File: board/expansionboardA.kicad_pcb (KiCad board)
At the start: 2 copper layers, 131 x 83.8 mm, 83 parts, among them J1 USB_C_Receptacle, J2 USB_A_Stacked, J3 HDMI_A, J4 USB_C_Receptacle, SW1 ESPPROG, U1 MAX3420EECJ, U2 GPIO_U2, U3 SII164CTG64, U4 GPIO_U4, U5 ESP32-C6-WROOM-1-N8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

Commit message: Updated board with 2 more pins between ESP32 and FPGA
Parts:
- SW1: moved to B.Cu
- moved REF** 18.4 mm to (65.0, 100.2)
- moved SW1 3.72 mm to (75.2, 118.8)
- moved REF** 3.04 mm to (35.8, 119.8)
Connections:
- U2 pad 25: unconnected-(U2-Pin_25-Pad25) -> IO11
- U2 pad 26: unconnected-(U2-Pin_26-Pad26) -> IO10
- U5 pad 11: unconnected-(U5-IO10-Pad11) -> IO10
- U5 pad 12: unconnected-(U5-IO11-Pad12) -> IO11
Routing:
- net IO11: track 0.00 -> 13.3 mm
- net IO10: track 0.00 -> 11.5 mm
- net REG3V3: track 340.7 -> 342.1 mm
- net Net-(U5-IO9): track 43.5 -> 42.4 mm, vias 1 -> 2
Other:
- board text added: "ESP32 DOWNLOAD"
- board text added: "K13"
- board text added: "K14"
- board text removed: "ESP32 DOWNLOAD MODE"

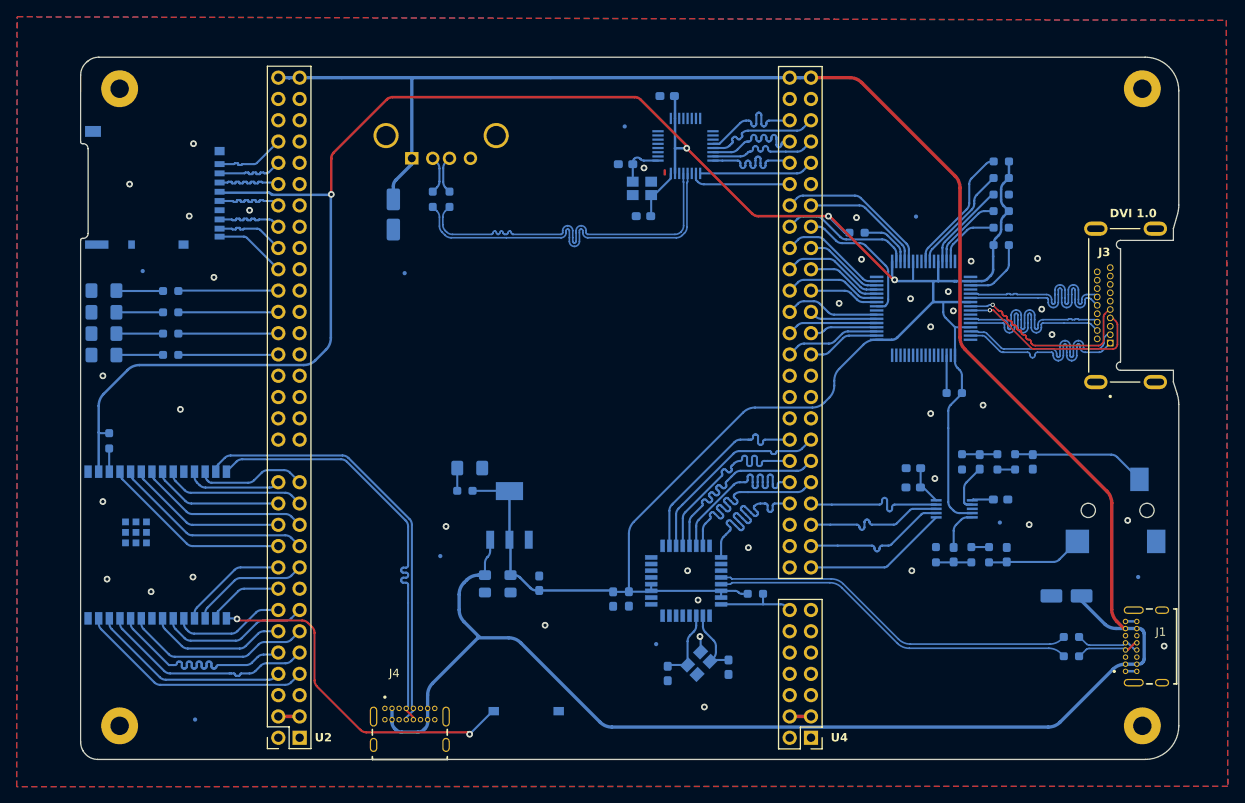
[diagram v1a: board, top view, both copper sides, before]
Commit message: Updated gateware, ROM version, and board schematic to remove MAX3420 support
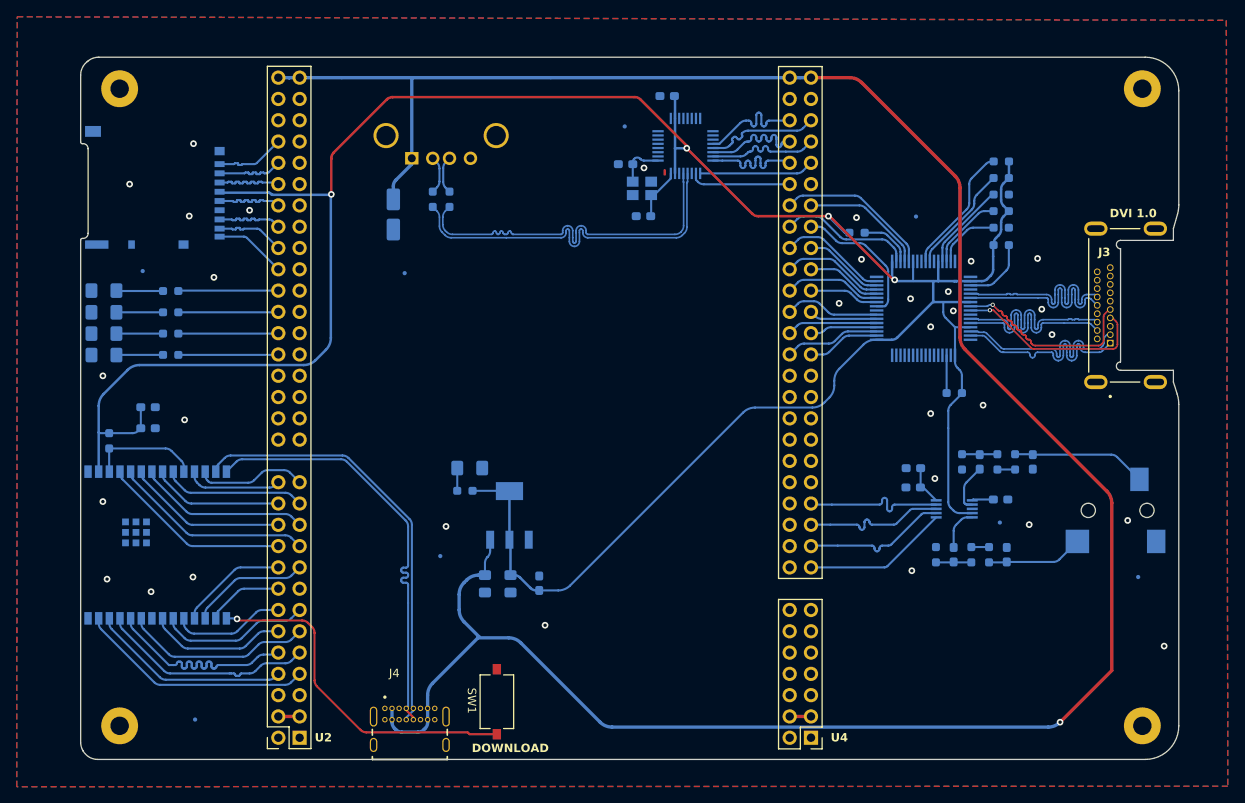
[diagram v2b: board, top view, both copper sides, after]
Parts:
- removed C3, C4: 18pf, Capacitor_SMD:C_0603_1608Metric_Pad1.08x0.95mm_HandSolder
- removed C5: 4.7uf, Capacitor_SMD:CP_Elec_4x5.4
- removed J1: USB_C_Receptacle, USB4085-GF-A_REVA4:GCT_USB4085-GF-A_REVA4
- removed R10, R9: 33Ohm, Resistor_SMD:R_0603_1608Metric_Pad0.98x0.95mm_HandSolder
- removed R2: 10KOhm, Resistor_SMD:R_0603_1608Metric_Pad0.98x0.95mm_HandSolder
- removed the REF** at (90.8, 110.8)
- removed U1: MAX3420EECJ, MAX3420EECJ:QFP80P900X900X160-32N
- removed Y1: 403C35D12M00000, 403C35D12M00000:XTAL_403C35D12M00000
- SW1: moved to F.Cu
- moved C2 60.9 mm to (30.1, 85.0), turned to 180 degrees
- moved C1 60.0 mm to (30.1, 82.5), turned to 180 degrees
- moved SW1 3.68 mm to (71.8, 117.6), turned to -90 degrees
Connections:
- U4 pad 24: INT -> unconnected-(U4-Pin_24-Pad24)
- U4 pad 25: USBGPX -> unconnected-(U4-Pin_25-Pad25)
- U4 pad 26: USBMOSI -> unconnected-(U4-Pin_26-Pad26)
- U4 pad 27: USBMISO -> unconnected-(U4-Pin_27-Pad27)
- U4 pad 28: USBSS -> unconnected-(U4-Pin_28-Pad28)
- U4 pad 29: USBSCLK -> unconnected-(U4-Pin_29-Pad29)
- U4 pad 30: USBRES -> unconnected-(U4-Pin_30-Pad30)
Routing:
- net USBD_P: track 44.3 -> 0.00 mm
- net USBD_N: track 44.2 -> 0.00 mm
- net USBSCLK: track 24.0 -> 0.00 mm
- net USBRES: track 24.0 -> 0.00 mm
- net USBGPX: track 23.9 -> 0.00 mm
- net USBMISO: track 23.9 -> 0.00 mm
- net USBMOSI: track 23.9 -> 0.00 mm
- net USBSS: track 23.9 -> 0.00 mm
- net INT: track 23.8 -> 0.00 mm
- net REG3V3: track 342.1 -> 328.0 mm
- net 5V: track 296.9 -> 284.4 mm, vias 0 -> 1
- net Net-(U5-EN): track 2.78 -> 13.3 mm
- net GPI: track 9.66 -> 0.00 mm
- net Net-(U1-XI): track 8.77 -> 0.00 mm
- net Net-(U1-XO): track 8.64 -> 0.00 mm
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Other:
- board text added: "DOWNLOAD"
- board text removed: "ESP32 DOWNLOAD"
- board text removed: "J4"
- board text removed: "K3"
- board text removed: "M2"

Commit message: Updated PCB
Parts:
- moved C17 29.3 mm to (97.4, 82.6)
- moved C6 27.2 mm to (92.9, 84.6)
- moved C7 27.2 mm to (89.8, 84.6)
- moved D1 27.2 mm to (88.0, 70.8)
- moved R1 27.2 mm to (87.4, 73.5)
- moved VR1 27.2 mm to (92.8, 76.4)
- moved REF** 26.5 mm to (85.4, 83.4)
- moved C20 2.75 mm to (56.7, 60.0), turned to 180 degrees
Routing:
- net 5V: track 284.4 -> 181.8 mm, vias 1 -> 0
- net REG3V3: track 328.0 -> 298.7 mm
- net GND: vias 32 -> 34
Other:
- board text added: "tinysys issue 2F April 2024 Engin Cilasun"
- board text removed: "tinysys issue 2E March 2024 Engin Cilasun"

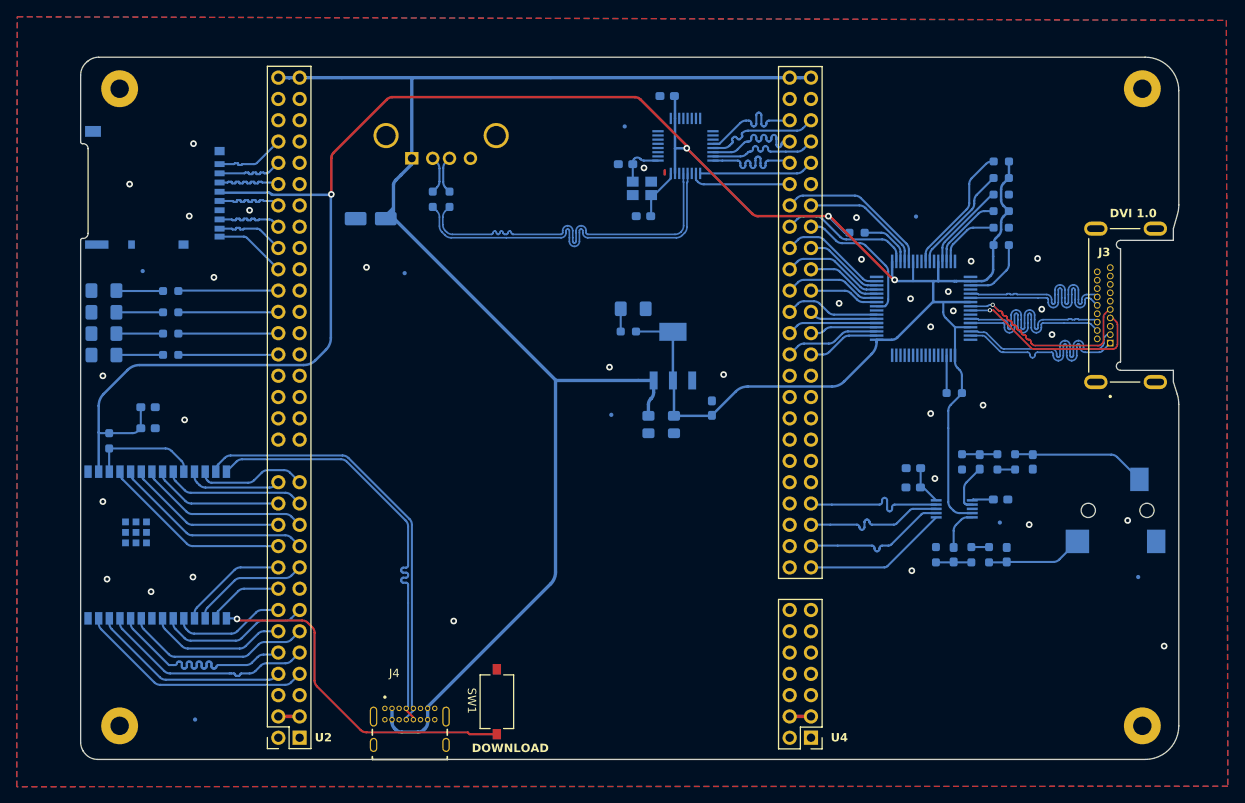
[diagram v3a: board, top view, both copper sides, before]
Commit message: Timing fixes Board updates
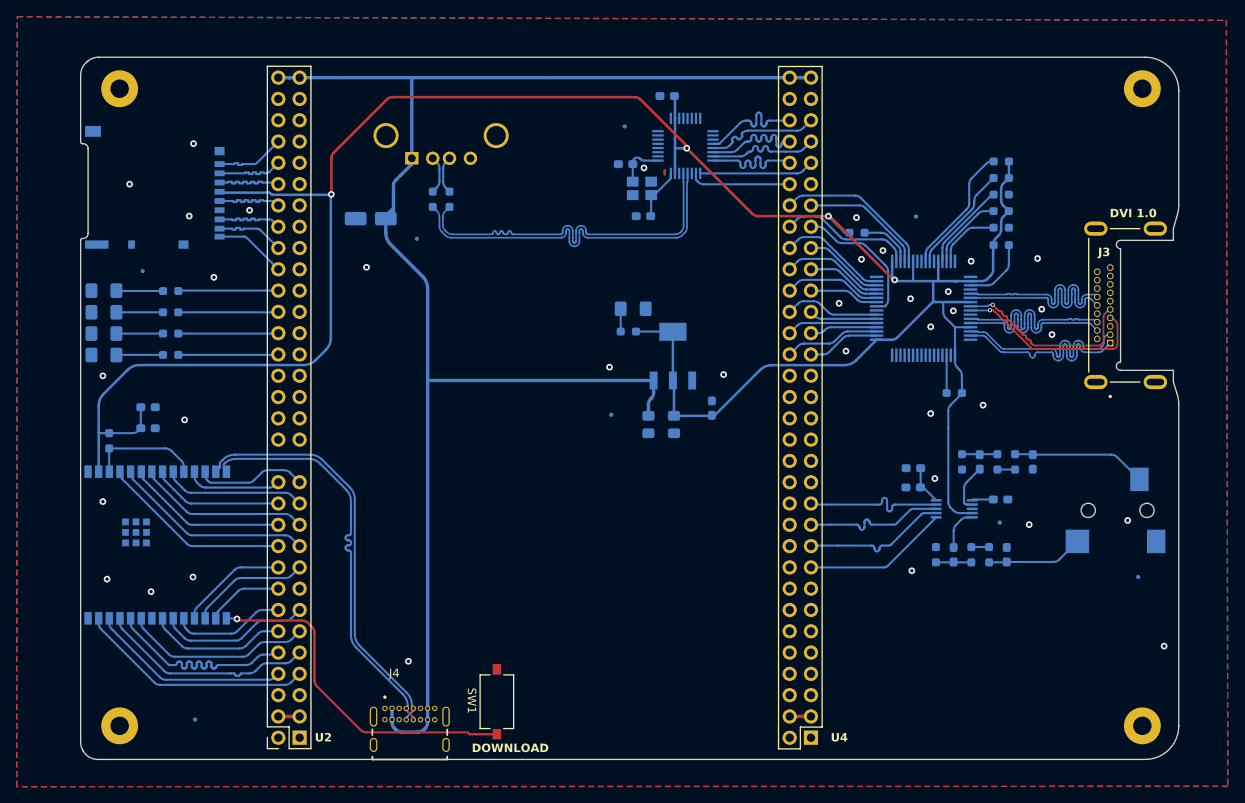
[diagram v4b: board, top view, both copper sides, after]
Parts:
- moved REF** 4.35 mm to (62.2, 62.4)
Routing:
- net ESPD_N: track 51.7 -> 49.5 mm
- net ESPD_P: track 51.6 -> 49.5 mm
- net 5V: track 181.8 -> 183.8 mm
- net REG3V3: track 298.7 -> 298.1 mm
- net GND: vias 34 -> 36

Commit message: More changes to sample
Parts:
- added U1: XC7A35T-FTG256, Package_BGA:Xilinx_FTG256, B.Cu at (84.7, 99.1)
- moved D1 14.6 mm to (97.8, 81.6), turned to 0 degrees
- moved R1 12.2 mm to (98.3, 78.9), turned to 0 degrees
- moved C6 6.70 mm to (92.9, 77.9)
- moved C7 6.70 mm to (89.9, 77.9)
- moved VR1 6.70 mm to (92.8, 69.7)
- moved C17 6.70 mm to (97.5, 75.9)
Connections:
- U4 pad 15: (no net) -> unconnected-(U4-Pin_15-Pad15)
- U4 pad 16: (no net) -> unconnected-(U4-Pin_16-Pad16)
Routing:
- net REG3V3: track 298.1 -> 293.7 mm
- net GND: vias 36 -> 35
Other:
- board text removed: "FPGA Data"

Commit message: undo board change
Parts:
- removed U1: XC7A35T-FTG256, Package_BGA:Xilinx_FTG256
